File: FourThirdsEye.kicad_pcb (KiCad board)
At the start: 4 copper layers, 47.1 x 45 mm, 116 parts, among them J1 QWIIC_CONNECTORJS-1MM, J3 Conn_Coaxial, J4 Conn_Coaxial, J5 Conn_Coaxial, J9 Conn_01x22_Female, U1 AP3418KTR-G1, U2 IMX294, U3 LP5907MFX-1.8, U4 TPS7A90, U5 ECS-2520MV-240-DN-TR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

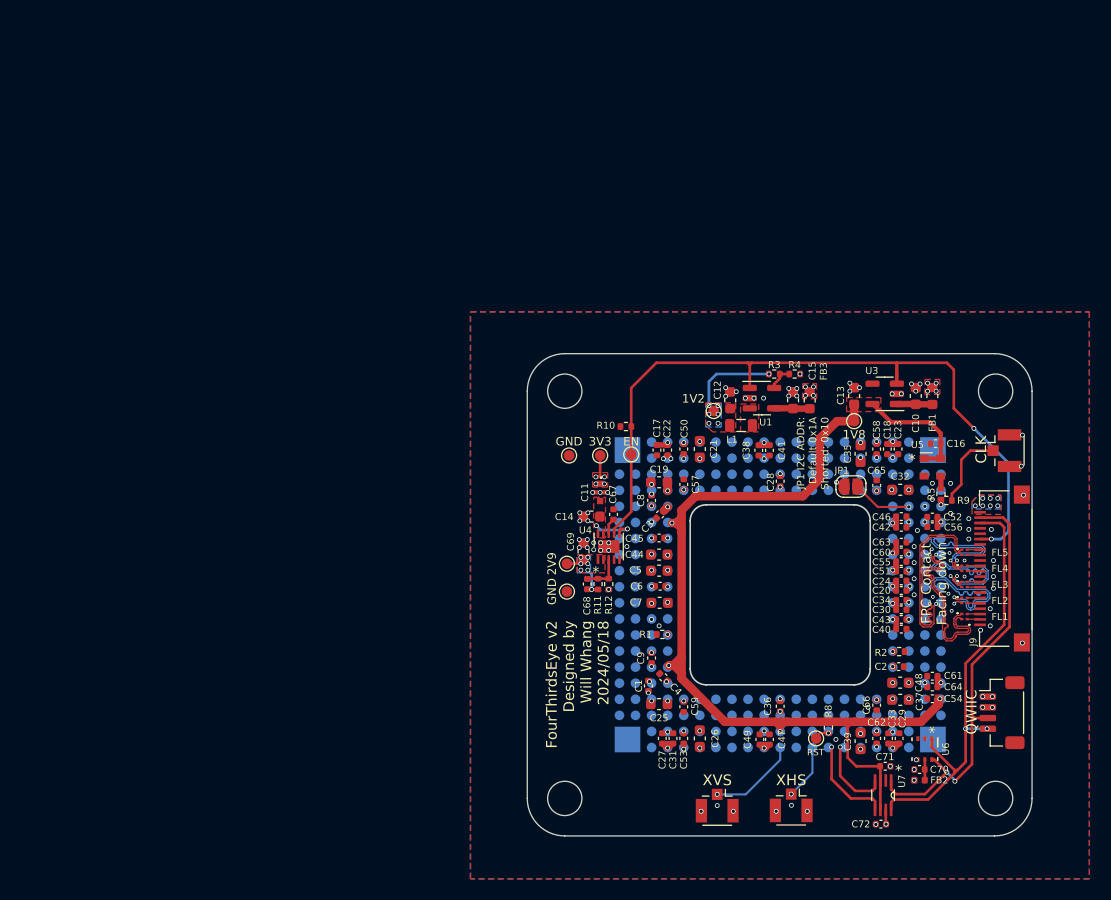
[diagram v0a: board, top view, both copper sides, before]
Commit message: upload V2.1 files and Cmount adaptor 3D model
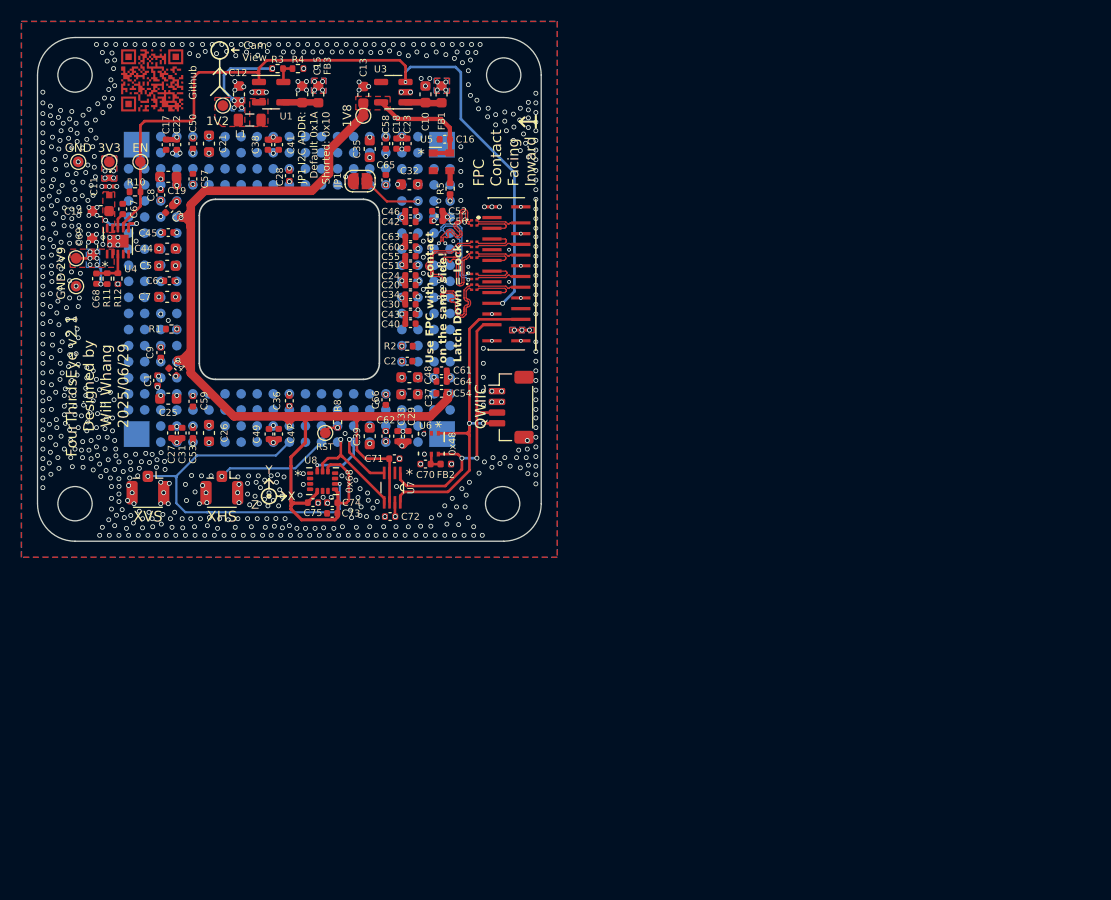
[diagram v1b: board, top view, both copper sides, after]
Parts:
- removed J5: Conn_Coaxial, Connector_Coaxial:U.FL_Hirose_U.FL-R-SMT-1_Vertical
- removed R9: DNP, Resistor_SMD:R_0402_1005Metric
- added ?: , clipboard:4c8eaa63-f78d-47fc-87d8-38423f66d82f, F.Cu at (87.2, 47.3)
- added C73: 100nF, Capacitor_SMD:C_0402_1005Metric, F.Cu at (103.2, 89.9)
- added C74: 10nF, Capacitor_SMD:C_0402_1005Metric, F.Cu at (103.2, 88.9)
- added C75: 1uF, Capacitor_SMD:C_0402_1005Metric, F.Cu at (101.4, 88.9)
- added U8: ICM-42688-P, footprints:PQFN50P300X250X97-14N, F.Cu at (102.3, 86.9)
- C67: value 10nF -> 1uF
- J1: value QWIIC_CONNECTORJS-1MM -> Conn_01x04_Shielded
- J9: footprint footprints:XF2M22151A -> footprints:TF3822S05SV830
- moved J3 60.8 mm to (86.0, 87.5)
- moved J4 60.8 mm to (92.9, 87.5)
- moved FL1 58.7 mm to (116.5, 62.8)
- moved FL2 56.5 mm to (116.5, 64.8)
- moved J9 55.4 mm to (117.8, 67.5)
- moved FL3 55.1 mm to (116.5, 65.8)
- moved H2 54.6 mm to (119.2, 49.0)
- moved R3 54.4 mm to (98.1, 48.4)
- moved R4 54.4 mm to (100.0, 48.4)
- moved H3 54.4 mm to (79.2, 49.0)
- moved C52 54.3 mm to (113.0, 61.7)
- moved C56 54.3 mm to (113.0, 62.6)
- moved C70 54.2 mm to (111.9, 85.3)
- moved U6 54.2 mm to (112.5, 83.4)
- moved C7 54.1 mm to (87.8, 69.7)
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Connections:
- FL1 pad 1: CAM_D0_P -> CAM_D0_N
- FL1 pad 2: /CAM1_D0_P -> /CAM1_D0_N
- FL1 pad 3: /CAM1_D0_N -> /CAM1_D0_P
- FL1 pad 4: CAM_D0_N -> CAM_D0_P
- FL2 pad 1: CAM_D1_P -> CAM_D1_N
- FL2 pad 2: /CAM1_D1_P -> /CAM1_D1_N
- FL2 pad 3: /CAM1_D1_N -> /CAM1_D1_P
- FL2 pad 4: CAM_D1_N -> CAM_D1_P
- FL3 pad 1: CAM_CLK_P -> CAM_CLK_N
- FL3 pad 2: /CAM1_CLK_P -> /CAM1_CLK_N
- FL3 pad 3: /CAM1_CLK_N -> /CAM1_CLK_P
- FL3 pad 4: CAM_CLK_N -> CAM_CLK_P
- FL4 pad 1: CAM_D2_P -> CAM_D2_N
- FL4 pad 2: /CAM1_D2_P -> /CAM1_D2_N
- FL4 pad 3: /CAM1_D2_N -> /CAM1_D2_P
- FL4 pad 4: CAM_D2_N -> CAM_D2_P
- FL5 pad 1: CAM_D3_P -> CAM_D3_N
- FL5 pad 2: /CAM1_D3_P -> /CAM1_D3_N
- FL5 pad 3: /CAM1_D3_N -> /CAM1_D3_P
- FL5 pad 4: CAM_D3_N -> CAM_D3_P
- J1 pad MP: (no net) -> GND
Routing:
- net XVS: track 8.36 -> 35.8 mm, vias 1 -> 2
- net +1V8: track 113.2 -> 139.8 mm
- net SDA_3V3: track 41.1 -> 27.9 mm
- net SCL_3V3: track 41.5 -> 33.1 mm
- net CAM_D3_N: track 16.3 -> 8.59 mm
- net CAM_D0_P: track 16.2 -> 8.56 mm
- net CAM_D0_N: track 16.2 -> 8.58 mm
- net Net-(J5-Pad1): track 7.49 -> 0.00 mm
- net CAM_D3_P: track 16.3 -> 9.02 mm
- net XHS: track 5.16 -> 10.6 mm
- net CAM_CLK_N: track 13.2 -> 8.62 mm
- net CAM_CLK_P: track 13.2 -> 8.60 mm
- net CAM_D1_N: track 13.0 -> 8.58 mm
- net /CAM1_D2_P: track 1.15 -> 5.26 mm
- net /CAM1_D3_N: track 1.15 -> 5.20 mm
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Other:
- board size 47.1 x 45 mm -> 47 x 47 mm
- board text added: "0x48"
- board text added: "0x68"
- board text added: "Cam View"
- board text added: "FPC Contact Facing Inward"
- board text added: "FourThirdsEye v2.1 Designed by Will Whang 2025/06/29"
- board text added: "Github"
- board text added: "Latch Down = Lock"
- board text added: "Use FPC with contact on the same side!"
- board text added: "X"
- board text added: "Y"
- board text added: "Z"
- board text removed: "CLK"
- board text removed: "FPC Contact Facing down"
- board text removed: "FourThirdsEye v2 Designed by Will Whang 2024/05/18"
